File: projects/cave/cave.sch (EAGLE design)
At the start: 111 parts, among them U1 IRLML6344TRPBF, U10 IRLML6344TRPBF, U11 IRLML6344TRPBF, U12 IRLML6344TRPBF, U2 TLC555CDR, U3 IRLML6344TRPBF, U4 IRLML6344TRPBF, U5 IRLML6344TRPBF, U6 IRLML6344TRPBF, U7 TPS54625, U9 IRLML6344TRPBF

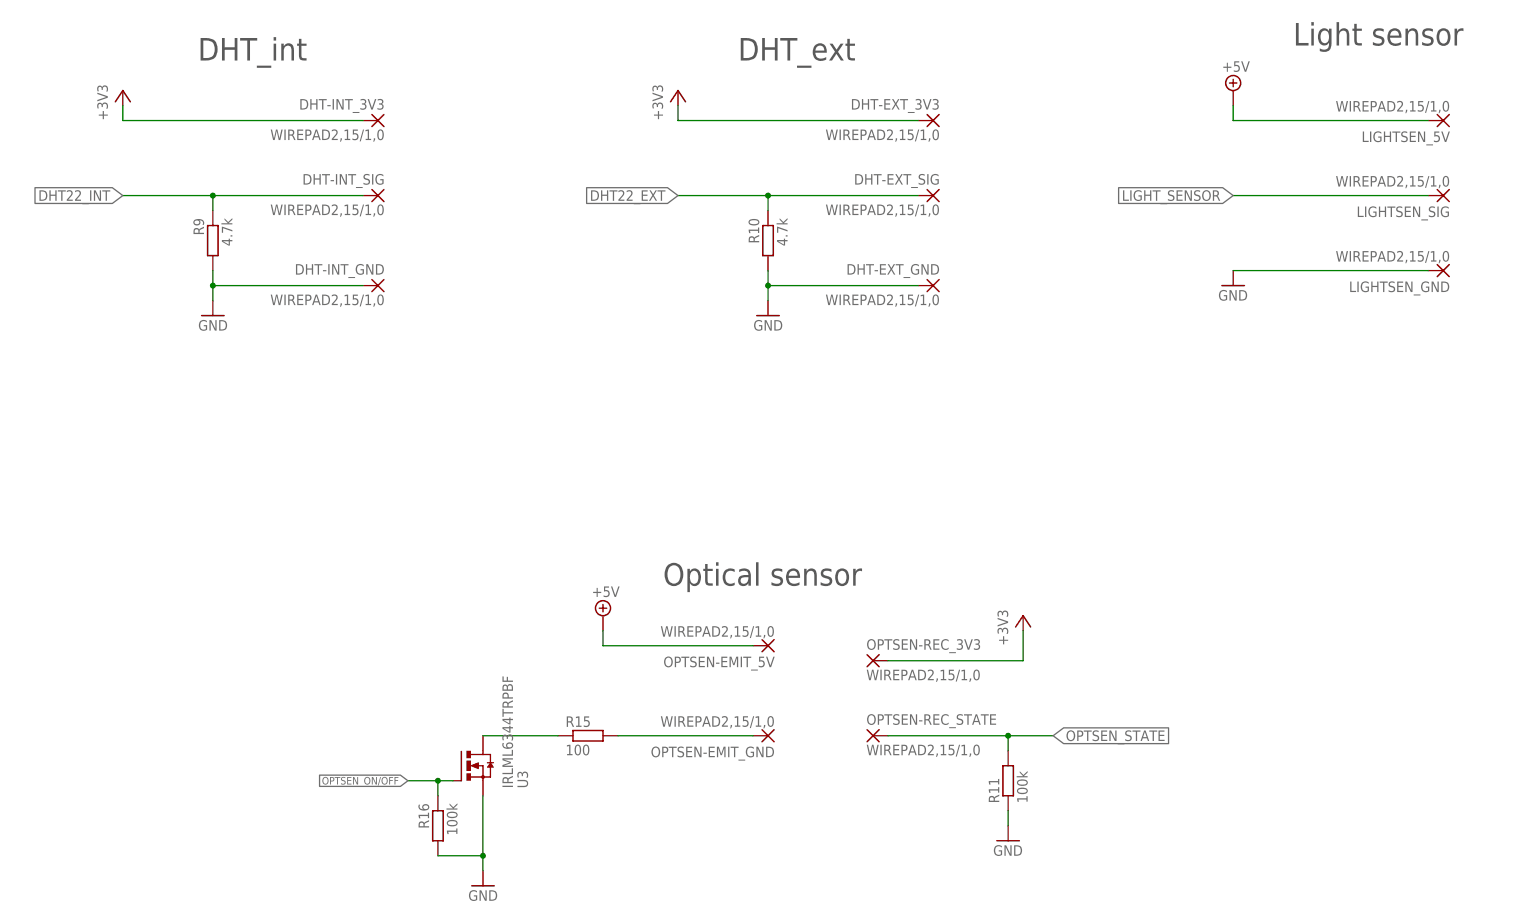
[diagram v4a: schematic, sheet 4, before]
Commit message: Reset lever circuit added to schematic and board ! BOM updated.
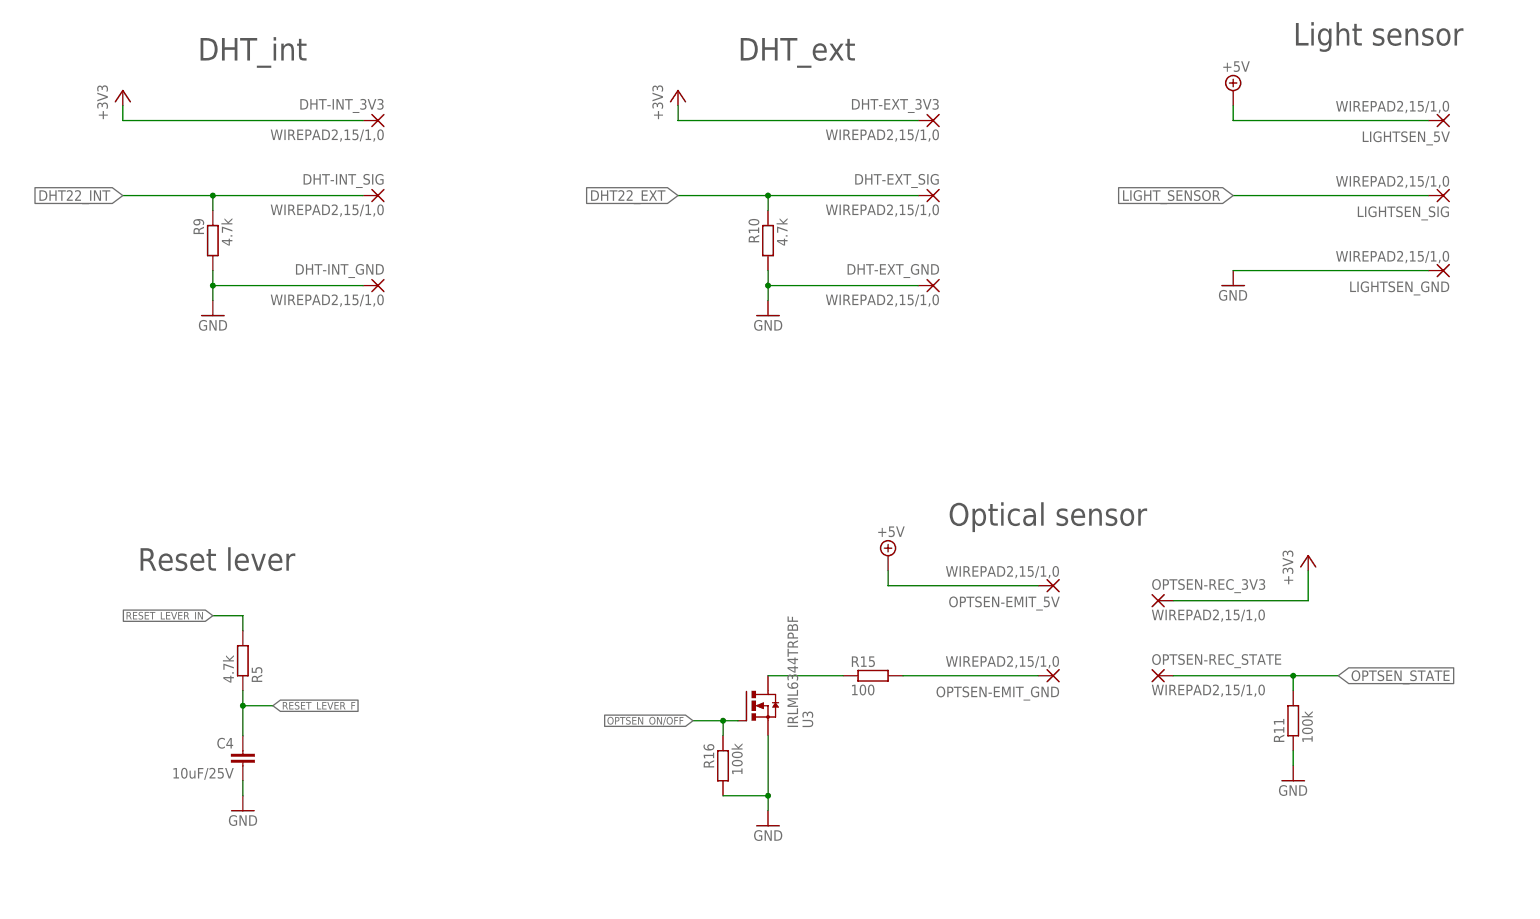
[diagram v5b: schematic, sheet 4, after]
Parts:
- added C4: 10uF/25V, rcl:C-EUC0805
- added R5: 4.7k, rcl:R-EU_R0603
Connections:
- removed net SPI_CE1: SV1.26, X2.5
- new net RESET_LEVER_F: C4.1, R5.1, SV1.26
- new net RESET_LEVER_IN: R5.2, X3.18
- net +3V3: now also X3.17
- net GND: now also C4.2, X2.5; no longer X3.17, X3.18
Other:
- note added: "Reset lever"
- moved on the sheet: OPTSEN-EMIT_5V, OPTSEN-EMIT_GND, OPTSEN-REC_3V3, OPTSEN-REC_STATE, R11, R15, R16, U3
